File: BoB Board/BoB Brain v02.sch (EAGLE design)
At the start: 41 parts, among them CN1 USB_CON, Q1 MOSFET-NCHANNELAO3404A, Q9 MOSFET-NCHANNELAO3404A, U1 ATMEGA328P_TQFP, U2 CH340G, U3 +12v, U4 V_REG_317SMD, Y1 16MHZ

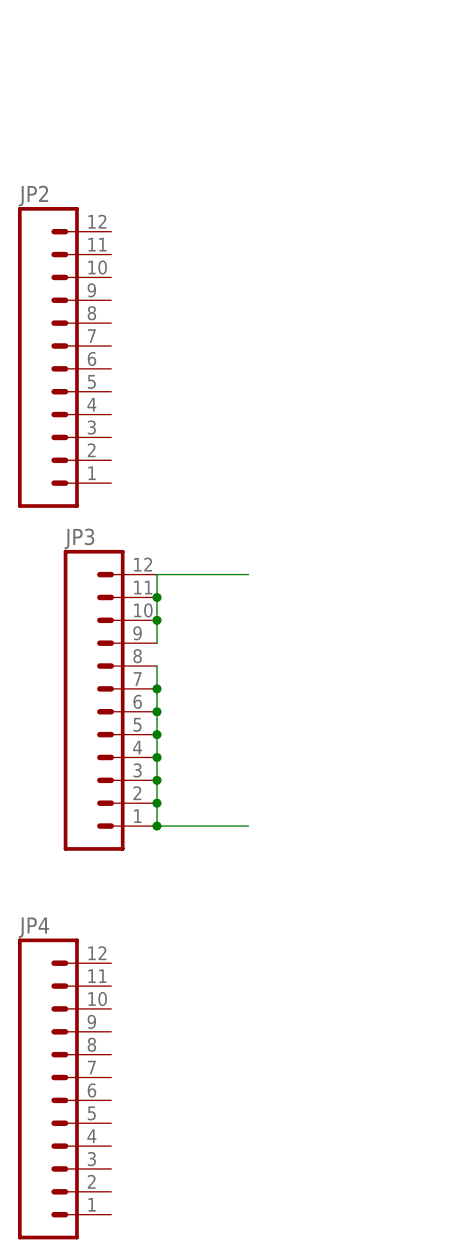
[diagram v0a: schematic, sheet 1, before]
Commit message: Added servo / digital power rails
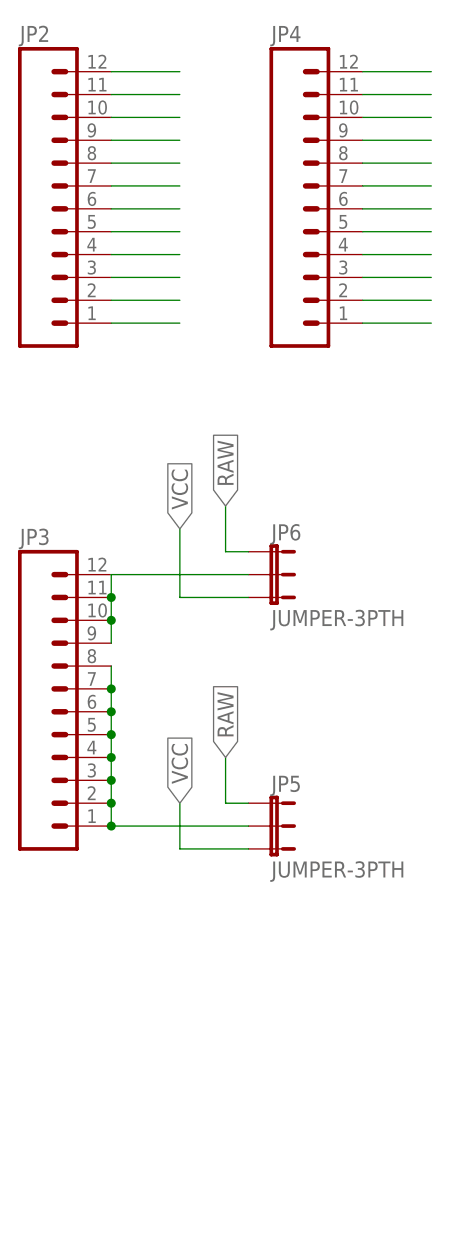
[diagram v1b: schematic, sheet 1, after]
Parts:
- added JP5, JP6: JUMPER-3PTH, SparkFun-Retired:JUMPER-3PTH
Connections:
- new net N$10: JP4.11
- new net N$16: JP4.10
- new net N$17: JP4.9
- new net N$18: JP4.8
- new net N$19: JP4.7
- new net N$20: JP4.6
- new net N$21: JP4.5
- new net N$22: JP4.4
- new net N$23: JP4.3
- new net N$24: JP4.2
- new net N$25: JP4.1
- new net N$7: JP4.12
- new net PIN_PWR: JP3.1, JP3.2, JP3.3, JP3.4, JP3.5, JP3.6, JP3.7, JP3.8, JP5.2
- new net RAW: C1.1, JP1.2, JP5.1, JP6.1, U3.IN
- net 6V: now also JP6.2; no longer C1.1, JP1.2, U3.IN
- net GND: now also JP2.1, JP2.10, JP2.11, JP2.12, JP2.2, JP2.3, JP2.4, JP2.5, JP2.6, JP2.7, JP2.8, JP2.9
- net VCC: now also JP5.3, JP6.3; no longer JP3.1, JP3.2, JP3.3, JP3.4, JP3.5, JP3.6, JP3.7, JP3.8
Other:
- moved on the sheet: JP2, JP3, JP4

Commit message: Working on BoB Board
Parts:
- removed C6, C7: 22pF, resistor:C-USC0805K
- removed C9: 0.1uF, resistor:C-USC0805K
- removed CN1: USB_CON, adafruit:USBMINIB
- removed R10, R16: 3.3k, resistor:R-US_R0805W
- removed R15: 10k, resistor:R-US_R0805W
- removed R23: 20k, resistor:R-US_R0805W
- removed RESONATOR: 16mhz, crystal:CRYSTALHC49UP
- removed U2: CH340G, usb-serial:CH340G
- added R1, R2: 1K, resistor:R-US_R0805W
- U$1: value ESP8266-07 -> HM-11; device lio:ESP8266-07 -> HM-11-ladvien:HM-11
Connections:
- removed net 12: R15.2, R23.2, U1.PB4(MISO)
- removed net D+: CN1.D+, U2.D+
- removed net D-: CN1.D-, U2.D-
- removed net ESP-RX: Q9.D, R19.1, U1.PD7(AIN1)
- removed net ESP-TX: Q1.D, R20.1, U1.PD6(AIN0)
- removed net X0: C7.1, RESONATOR.2, U2.XO
- removed net X1: C6.1, RESONATOR.1, U2.XI
- new net ATMEGA-RESET: R2.1, U$1.14-PIO2
- new net HM-RESET: R1.1, U1.PD2(INT0)
- new net N$26: U1.PC5(ADC5/SCL)
- new net N$27: U1.ADC6
- new net N$28: U1.ADC7
- new net N$29: U1.PD3(INT1)
- new net N$30: U1.PD4(XCK/T0)
- new net N$31: U1.PD6(AIN0)
- new net N$32: U1.PD7(AIN1)
- new net N$33: U1.PB0(ICP)
- new net RESET: C5.2, R1.2, R14.1, R2.2, S1.3, S1.4, U$1.11-RESET, U1.PC6(/RESET)
- net 3.35V: now also U$1.9-VCC; no longer C9.1, R10.1, U$1.CH_PD, U$1.VCC
- net DTR: no longer U2.DTR
- net GND: now also U$1.12-GND; no longer C6.2, C7.2, C9.2, CN1.GND, R16.1, R23.1, U$1.GND, U2.GND
- net N$12: now also U$1.2-TX; no longer U$1.TXD
- net N$13: now also U1.PC4(ADC4/SDA); no longer C5.2, R14.1, S1.3, S1.4, U1.PC6(/RESET)
- net N$15: now also U$1.4-RX; no longer U$1.RXD
- net N$3: now also U1.PB4(MISO); no longer R15.1, U$1.REST
- net N$4: now also U1.PC0(ADC0); no longer R10.2, U$1.GPIO2
- net N$5: now also U1.PC3(ADC3); no longer R16.2, U$1.GPIO15
- net U2_RX: now also Q1.D, R20.1; no longer U2.RX
- net U2_TX: now also Q9.D, R19.1; no longer U2.TX
- net VCC: no longer CN1.VBUS, U2.VCC
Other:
- moved on the sheet: R19, R20, R21, R22
